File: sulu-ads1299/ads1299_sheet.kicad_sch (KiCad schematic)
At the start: 13 parts, among them U2 ADS1299_TQFP-64

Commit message: Sulu-ads1299 finalized floorplan, began routing, updated schematic
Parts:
- removed R3: 10K, Resistor_SMD:R_0402_1005Metric, symbol Device:R_Small_US
- C12, C13: footprint (none) -> Capacitor_SMD:C_0402_1005Metric
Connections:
- net ADS_CLKSEL is gone; now on net 1.8V_REG: U2.52 (CLKSEL)
- net AVSS is gone; now on net GND: U2.20 (AVSS), U2.23 (AVSS), U2.32 (AVSS)
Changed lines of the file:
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@@
-    (stroke (width 0) (type default) (color 0 0 0 0))
-  )
-  (wire (pts (xy 143.51 31.75) (xy 144.78 31.75))
     (stroke (width 0) (type default) (color 0 0 0 0))
   )
@@
     (stroke (width 0) (type default) (color 0 0 0 0))
   )
-  (wire (pts (xy 146.05 34.29) (xy 146.05 35.56))
-    (stroke (width 0) (type default) (color 0 0 0 0))
-  )
   (wire (pts (xy 104.14 40.64) (xy 105.41 40.64))
     (stroke (width 0) (type default) (color 0 0 0 0))
@@
     (stroke (width 0) (type default) (color 0 0 0 0))
   )
-  (wire (pts (xy 147.32 34.29) (xy 146.05 34.29))
-    (stroke (width 0) (type default) (color 0 0 0 0))
-  )
   (wire (pts (xy 62.23 114.3) (xy 62.23 115.57))
     (stroke (width 0) (type default) (color 0 0 0 0))
@@
     (stroke (width 0) (type default) (color 0 0 0 0))
   )
-  (wire (pts (xy 203.2 35.56) (xy 205.74 35.56))
-    (stroke (width 0) (type default) (color 0 0 0 0))
-  )
   (wire (pts (xy 66.04 27.94) (xy 57.15 27.94))
     (stroke (width 0) (type default) (color 0 0 0 0))
   )
-  (wire (pts (xy 147.32 30.48) (xy 147.32 34.29))
-    (stroke (width 0) (type default) (color 0 0 0 0))
-  )
   (wire (pts (xy 104.14 68.58) (xy 105.41 68.58))
     (stroke (width 0) (type default) (color 0 0 0 0))
@@
     (stroke (width 0) (type default) (color 0 0 0 0))
   )
-  (wire (pts (xy 205.74 29.21) (xy 205.74 30.48))
-    (stroke (width 0) (type default) (color 0 0 0 0))
-  )
   (wire (pts (xy 162.56 60.96) (xy 163.83 60.96))
     (stroke (width 0) (type default) (color 0 0 0 0))
   )
+  (wire (pts (xy 146.05 25.4) (xy 146.05 35.56))
+    (stroke (width 0) (type default) (color 0 0 0 0))
+  )
   (wire (pts (xy 128.27 85.09) (xy 128.27 86.36))
     (stroke (width 0) (type default) (color 0 0 0 0))
@@
     (stroke (width 0) (type default) (color 0 0 0 0))
   )
+  (wire (pts (xy 153.67 85.09) (xy 153.67 86.36))
+    (stroke (width 0) (type default) (color 0 0 0 0))
+  )
   (wire (pts (xy 57.15 27.94) (xy 57.15 30.48))
     (stroke (width 0) (type default) (color 0 0 0 0))
@@
     (stroke (width 0) (type default) (color 0 0 0 0))
   )
-  (wire (pts (xy 153.67 85.09) (xy 153.67 87.63))
-    (stroke (width 0) (type default) (color 0 0 0 0))
-  )
   (wire (pts (xy 90.17 97.79) (xy 90.17 109.22))
     (stroke (width 0) (type default) (color 0 0 0 0))
@@
     (stroke (width 0) (type default) (color 0 0 0 0))
   )
-  (wire (pts (xy 151.13 34.29) (xy 151.13 35.56))
+  (wire (pts (xy 151.13 25.4) (xy 151.13 35.56))
     (stroke (width 0) (type default) (color 0 0 0 0))
   )
@@
     (stroke (width 0) (type default) (color 0 0 0 0))
   )
+  (wire (pts (xy 143.51 34.29) (xy 143.51 35.56))
+    (stroke (width 0) (type default) (color 0 0 0 0))
+  )
   (wire (pts (xy 71.12 24.13) (xy 76.2 24.13))
     (stroke (width 0) (type default) (color 0 0 0 0))
   )
   (wire (pts (xy 76.2 24.13) (xy 76.2 27.94))
-    (stroke (width 0) (type default) (color 0 0 0 0))
-  )
-  (wire (pts (xy 143.51 31.75) (xy 143.51 35.56))
     (stroke (width 0) (type default) (color 0 0 0 0))
   )
@@
     (effects (font (size 1.27 1.27)) (justify left bottom))
   )
-  (label "AVSS" (at 130.81 86.36 270)
-    (effects (font (size 1.27 1.27)) (justify right bottom))
-  )
   (label "VCAP3" (at 59.69 101.6 180)
     (effects (font (size 1.27 1.27)) (justify right bottom))
@@
     (effects (font (size 1.27 1.27)) (justify right bottom))
   )
-  (label "DVDD" (at 151.13 34.29 90)
+  (label "DVDD" (at 151.13 25.4 90)
     (effects (font (size 1.27 1.27)) (justify left bottom))
   )
@@
     (effects (font (size 1.27 1.27)) (justify right bottom))
   )
-  (label "ADS_CLKSEL" (at 147.32 30.48 90)
-    (effects (font (size 1.27 1.27)) (justify left bottom))
-  )
   (label "AVDD" (at 120.65 86.36 270)
     (effects (font (size 1.27 1.27)) (justify right bottom))
   )
   (label "AVDD" (at 125.73 86.36 270)
-    (effects (font (size 1.27 1.27)) (justify right bottom))
-  )
-  (label "ADS_CLKSEL" (at 203.2 35.56 180)
-    (effects (font (size 1.27 1.27)) (justify right bottom))
-  )
-  (label "AVSS" (at 153.67 87.63 270)
     (effects (font (size 1.27 1.27)) (justify right bottom))
   )
@@
     (effects (font (size 1.27 1.27)) (justify left bottom))
   )
-  (label "AVSS" (at 123.19 86.36 270)
-    (effects (font (size 1.27 1.27)) (justify right bottom))
-  )
-  (label "DVDD" (at 205.74 29.21 90)
+  (label "DVDD" (at 146.05 25.4 90)
     (effects (font (size 1.27 1.27)) (justify left bottom))
   )
@@
     (pin "1")
   )
+  (symbol (lib_id "power:GND") (at 123.19 86.36 0) (unit 1)
+    (in_bom yes) (on_board yes)
+    (property "Reference" "#PWR?" (id 0) (at 123.19 92.71 0)
+      (effects (font (size 1.27 1.27)) hide)
+    )
+    (property "Value" "GND" (id 1) (at 123.19 91.44 90))
+    (property "Footprint" "" (id 2) (at 123.19 86.36 0)
+      (effects (font (size 1.27 1.27)) hide)
+    )
+    (property "Datasheet" "" (id 3) (at 123.19 86.36 0)
+      (effects (font (size 1.27 1.27)) hide)
+    )
+    (pin "1")
+  )
   (symbol (lib_id "Device:C_Small") (at 99.06 111.76 0) (unit 1)
     (in_bom yes) (on_board yes) (fields_autoplaced)
@@
       (effects (font (size 1.27 1.27)) (justify left))
     )
-    (property "Footprint" "" (id 2) (at 99.06 111.76 0)
+    (property "Footprint" "Capacitor_SMD:C_0402_1005Metric" (id 2) (at 99.06 111.76 0)
       (effects (font (size 1.27 1.27)) hide)
     )
@@
       (effects (font (size 1.27 1.27)) (justify left))
     )
-    (property "Footprint" "" (id 2) (at 90.17 111.76 0)
+    (property "Footprint" "Capacitor_SMD:C_0402_1005Metric" (id 2) (at 90.17 111.76 0)
       (effects (font (size 1.27 1.27)) hide)
     )
@@
     (pin "1")
     (pin "2")
+  )
+  (symbol (lib_id "power:GND") (at 130.81 86.36 0) (unit 1)
+    (in_bom yes) (on_board yes)
+    (property "Reference" "#PWR?" (id 0) (at 130.81 92.71 0)
+      (effects (font (size 1.27 1.27)) hide)
+    )
+    (property "Value" "GND" (id 1) (at 130.81 91.44 90))
+    (property "Footprint" "" (id 2) (at 130.81 86.36 0)
+      (effects (font (size 1.27 1.27)) hide)
+    )
+    (property "Datasheet" "" (id 3) (at 130.81 86.36 0)
+      (effects (font (size 1.27 1.27)) hide)
+    )
+    (pin "1")
   )
   (symbol (lib_id "power:GND") (at 132.08 31.75 0) (unit 1)
@@
     (pin "1")
   )
+  (symbol (lib_id "power:GND") (at 153.67 86.36 0) (unit 1)
+    (in_bom yes) (on_board yes)
+    (property "Reference" "#PWR?" (id 0) (at 153.67 92.71 0)
+      (effects (font (size 1.27 1.27)) hide)
+    )
+    (property "Value" "GND" (id 1) (at 153.67 91.44 90))
+    (property "Footprint" "" (id 2) (at 153.67 86.36 0)
+      (effects (font (size 1.27 1.27)) hide)
+    )
+    (property "Datasheet" "" (id 3) (at 153.67 86.36 0)
+      (effects (font (size 1.27 1.27)) hide)
+    )
+    (pin "1")
+  )
   (symbol (lib_id "Device:C_Small") (at 44.45 33.02 0) (unit 1)
     (in_bom yes) (on_board yes) (fields_autoplaced)
@@
     (pin "1")
   )
-  (symbol (lib_id "Device:R_Small_US") (at 205.74 33.02 0) (unit 1)
-    (in_bom yes) (on_board yes) (fields_autoplaced)
-    (property "Reference" "R3" (id 0) (at 208.28 31.7499 0)
-      (effects (font (size 1.27 1.27)) (justify left))
-    )
-    (property "Value" "10K" (id 1) (at 208.28 34.2899 0)
-      (effects (font (size 1.27 1.27)) (justify left))
-    )
-    (property "Footprint" "Resistor_SMD:R_0402_1005Metric" (id 2) (at 205.74 33.02 0)
-      (effects (font (size 1.27 1.27)) hide)
-    )
-    (property "Datasheet" "~" (id 3) (at 205.74 33.02 0)
-      (effects (font (size 1.27 1.27)) hide)
-    )
-    (pin "1")
-    (pin "2")
-  )
   (symbol (lib_id "power:GND") (at 99.06 116.84 0) (unit 1)
     (in_bom yes) (on_board yes) (fields_autoplaced)
@@
     (pin "1")
   )
-  (symbol (lib_id "power:GND") (at 144.78 31.75 0) (unit 1)
+  (symbol (lib_id "power:GND") (at 143.51 34.29 180) (unit 1)
     (in_bom yes) (on_board yes)
-    (property "Reference" "#PWR045" (id 0) (at 144.78 38.1 0)
-      (effects (font (size 1.27 1.27)) hide)
-    )
-    (property "Value" "GND" (id 1) (at 142.7581 30.8024 0)
-      (effects (font (size 1.27 1.27)) (justify left))
-    )
-    (property "Footprint" "" (id 2) (at 144.78 31.75 0)
-      (effects (font (size 1.27 1.27)) hide)
-    )
-    (property "Datasheet" "" (id 3) (at 144.78 31.75 0)
-      (effects (font (size 1.27 1.27)) hide)
-    )
+    (property "Reference" "#PWR045" (id 0) (at 143.51 27.94 0)
+      (effects (font (size 1.27 1.27)) hide)
+    )
+    (property "Value" "GND" (id 1) (at 143.51 26.67 90)
+      (effects (font (size 1.27 1.27)) (justify left))
+    )
+    (property "Footprint" "" (id 2) (at 143.51 34.29 0)
+      (effects (font (size 1.27 1.27)) hide)
+    )
+    (property "Datasheet" "" (id 3) (at 143.51 34.29 0)
+      (effects (font (size 1.27 1.27)) hide)
+    )

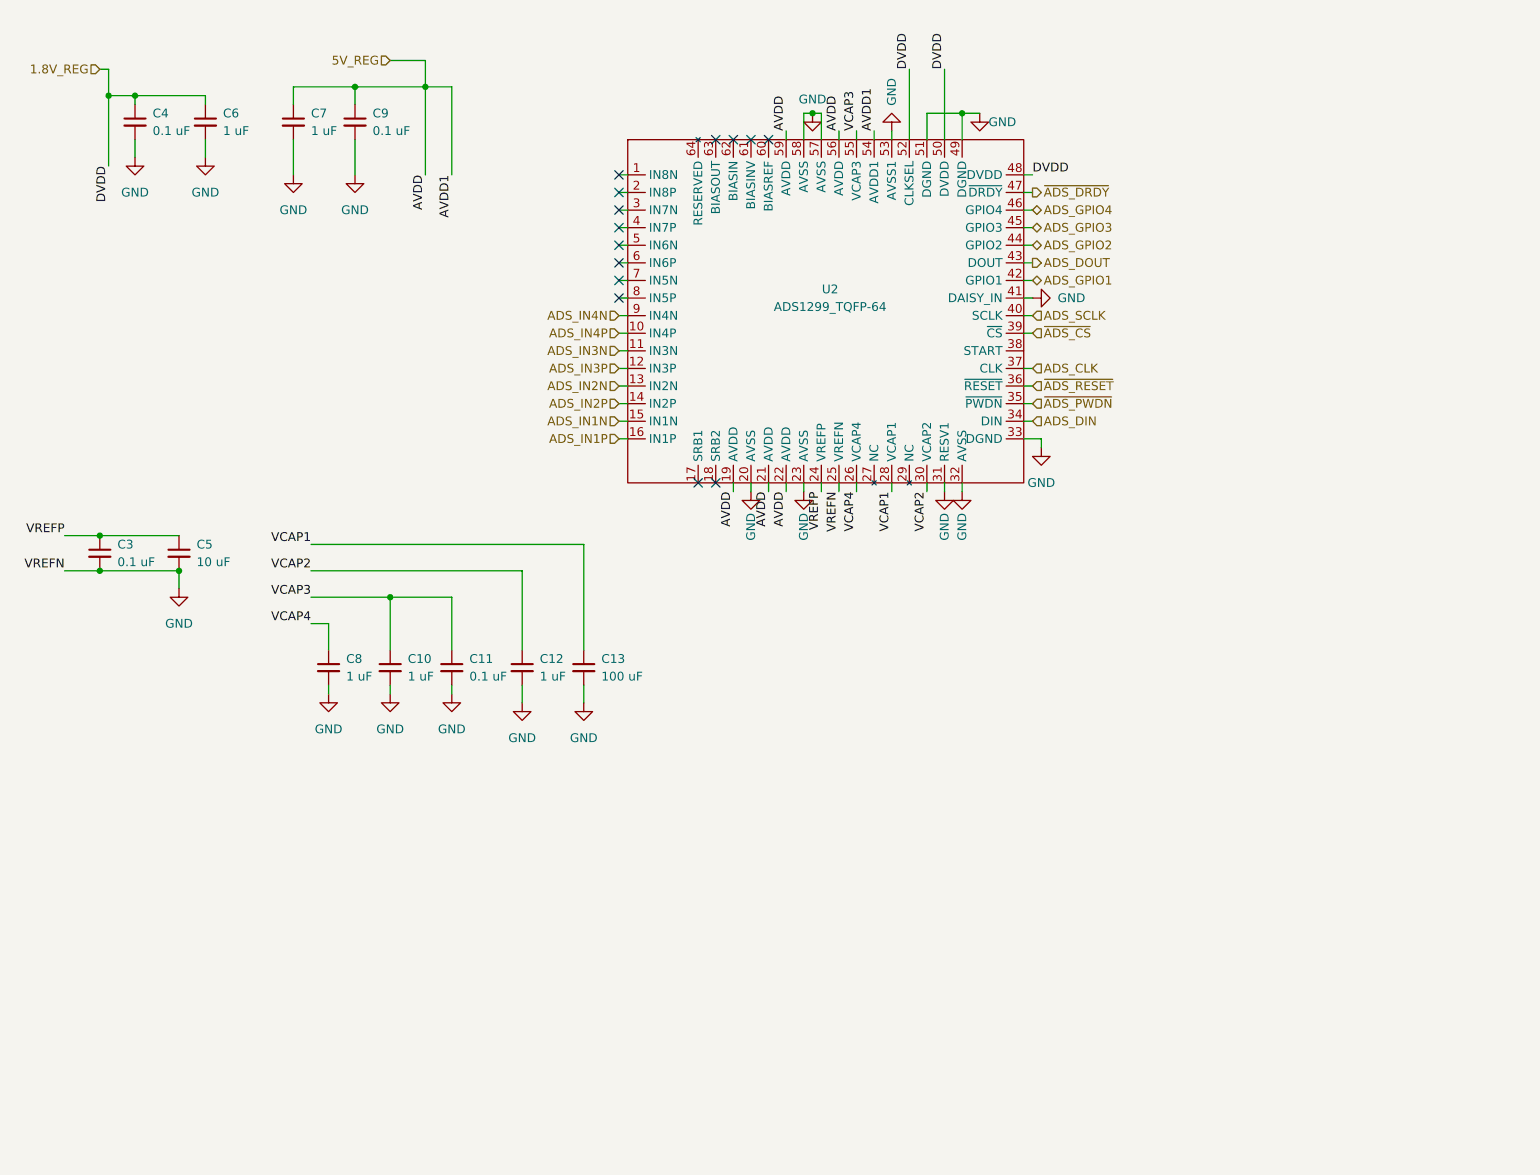
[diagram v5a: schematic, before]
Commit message: Sulu-ads1299, completed place & route
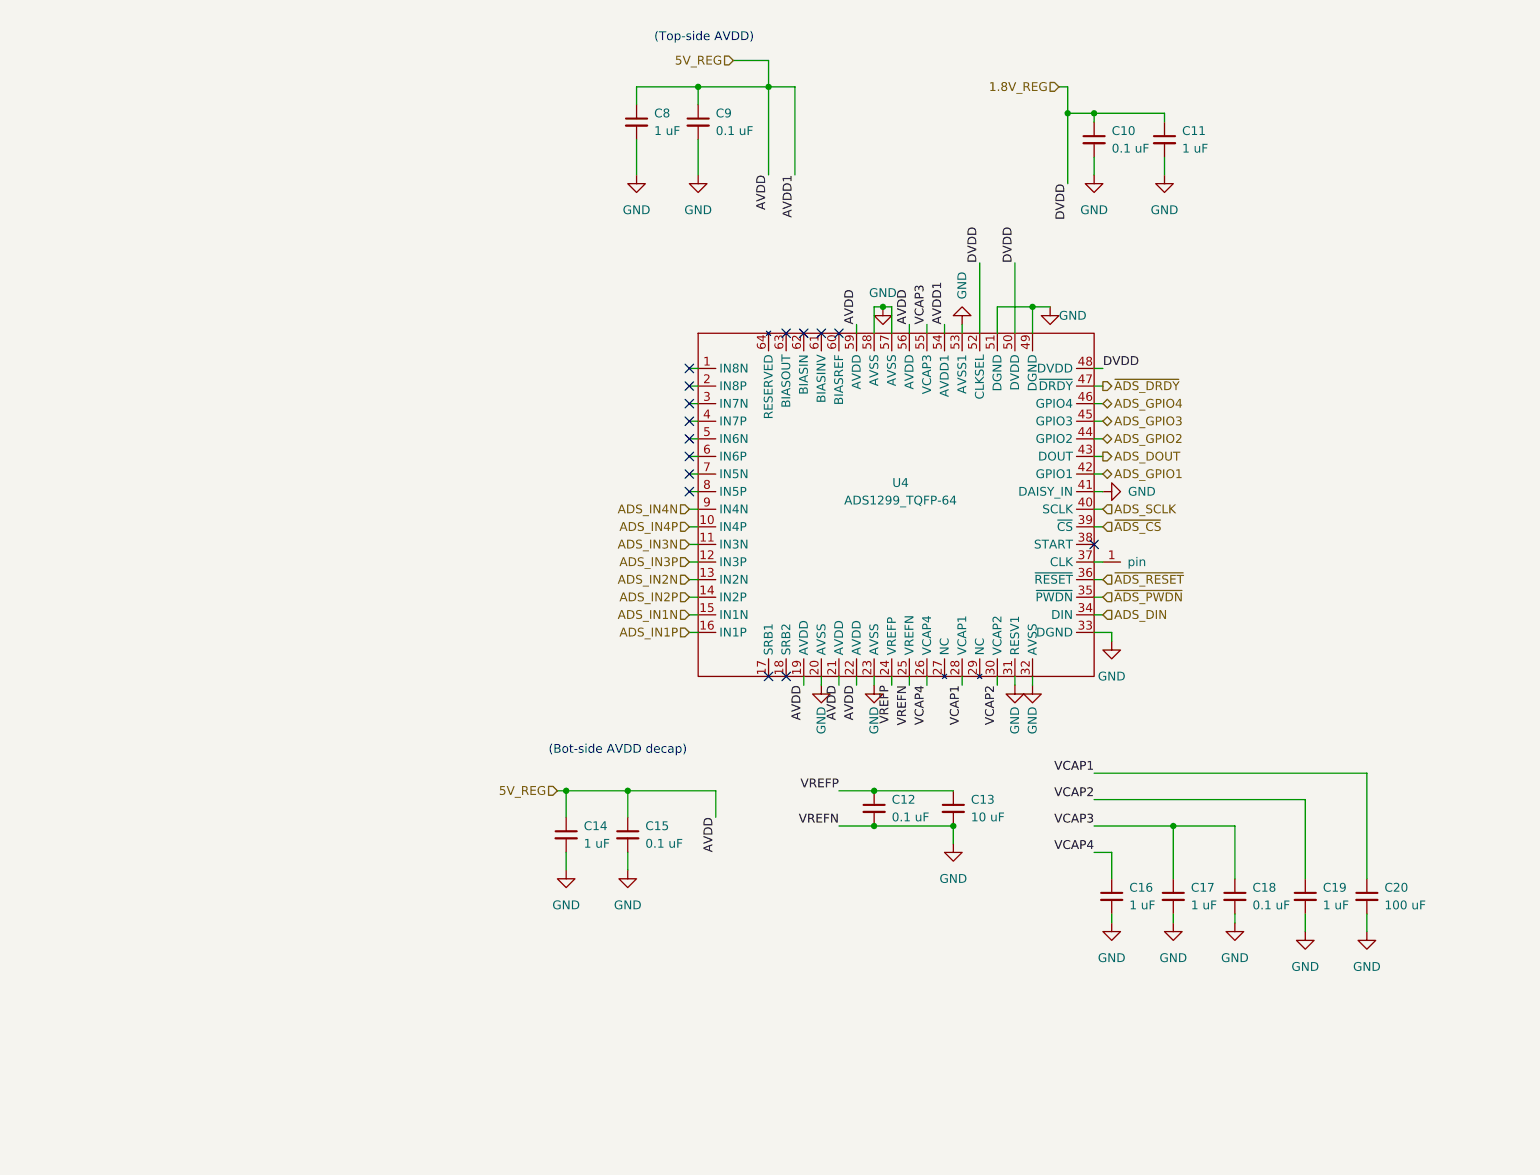
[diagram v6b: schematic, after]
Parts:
- added C14: 1 uF, Capacitor_SMD:C_0402_1005Metric, symbol Device:C_Small
- added C15: 0.1 uF, Capacitor_SMD:C_0402_1005Metric, symbol Device:C_Small
- added J8: through_hole, SCUM:through_hole, symbol draft1library:through_hole
- renumbered C4 to C10, C6 to C11, C3 to C12, C5 to C13, C8 to C16, C10 to C17, C11 to C18, C12 to C19, C13 to C20, C7 to C8, U2 to U4
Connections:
- net 5V_REG: now also C14.1, C15.1
- net GND: now also C14.2, C15.2
- net ADS_CLK: no longer names the net of U4.37 (CLK)
- net ADS_CLK: now also J8.1 (pin)
- no-connect marks 14 -> 15
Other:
- note added: "(Bot-side AVDD decap)"
- note added: "(Top-side AVDD)"
- moved on the sheet: C10, C11, C12, C13, C16, C17, C18, C19, C20, C8, C9, U4

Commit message: Upated schematic and layout.
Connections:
- net GND: now also U4.38 (START)
- no-connect marks 15 -> 14
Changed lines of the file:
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@@
   (no_connect (at 114.3 86.36))
   (no_connect (at 114.3 83.82))
-  (no_connect (at 172.72 93.98))
   (no_connect (at 125.73 113.03))
   (no_connect (at 128.27 63.5))
@@
     (stroke (width 0) (type default) (color 0 0 0 0))
   )
+  (wire (pts (xy 172.72 93.98) (xy 189.23 93.98))
+    (stroke (width 0) (type default) (color 0 0 0 0))
+  )
   (wire (pts (xy 172.72 83.82) (xy 173.99 83.82))
     (stroke (width 0) (type default) (color 0 0 0 0))
@@
   )
   (wire (pts (xy 172.72 31.75) (xy 182.88 31.75))
+    (stroke (width 0) (type default) (color 0 0 0 0))
+  )
+  (wire (pts (xy 189.23 93.98) (xy 189.23 96.52))
     (stroke (width 0) (type default) (color 0 0 0 0))
   )
@@
       (effects (font (size 1.27 1.27)) hide)
     )
+    (pin "1")
+  )
+  (symbol (lib_id "power:GND") (at 189.23 96.52 0) (unit 1)
+    (in_bom yes) (on_board yes) (fields_autoplaced)
+    (property "Reference" "#PWR0109" (id 0) (at 189.23 102.87 0)
+      (effects (font (size 1.27 1.27)) hide)
+    )
+    (property "Value" "GND" (id 1) (at 189.23 101.6 0))
+    (property "Footprint" "" (id 2) (at 189.23 96.52 0)
+      (effects (font (size 1.27 1.27)) hide)
+    )
+    (property "Datasheet" "" (id 3) (at 189.23 96.52 0)
+      (effects (font (size 1.27 1.27)) hide)
+    )

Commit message: Sulu-ADS1299 10uF DCDC output decap, BoM, and bigger C20 footprint
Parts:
- C20: footprint Capacitor_SMD:C_0402_1005Metric -> Capacitor_SMD:C_0805_2012Metric
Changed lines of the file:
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@@
       (effects (font (size 1.27 1.27)) (justify left))
     )
-    (property "Footprint" "Capacitor_SMD:C_0402_1005Metric" (id 2) (at 212.09 144.78 0)
+    (property "Footprint" "Capacitor_SMD:C_0805_2012Metric" (id 2) (at 212.09 144.78 0)
       (effects (font (size 1.27 1.27)) hide)
     )
